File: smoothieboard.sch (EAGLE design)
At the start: 235 parts, among them IC1 LPC1769, IC10 LM1117-3.3V, IC11 78L12F, IC2 A4982, IC3 A4982, IC4 MCP44X1, IC5 A4982, IC6 A4982, J10 POWER_JACKSMD, Q1 BSL207SP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

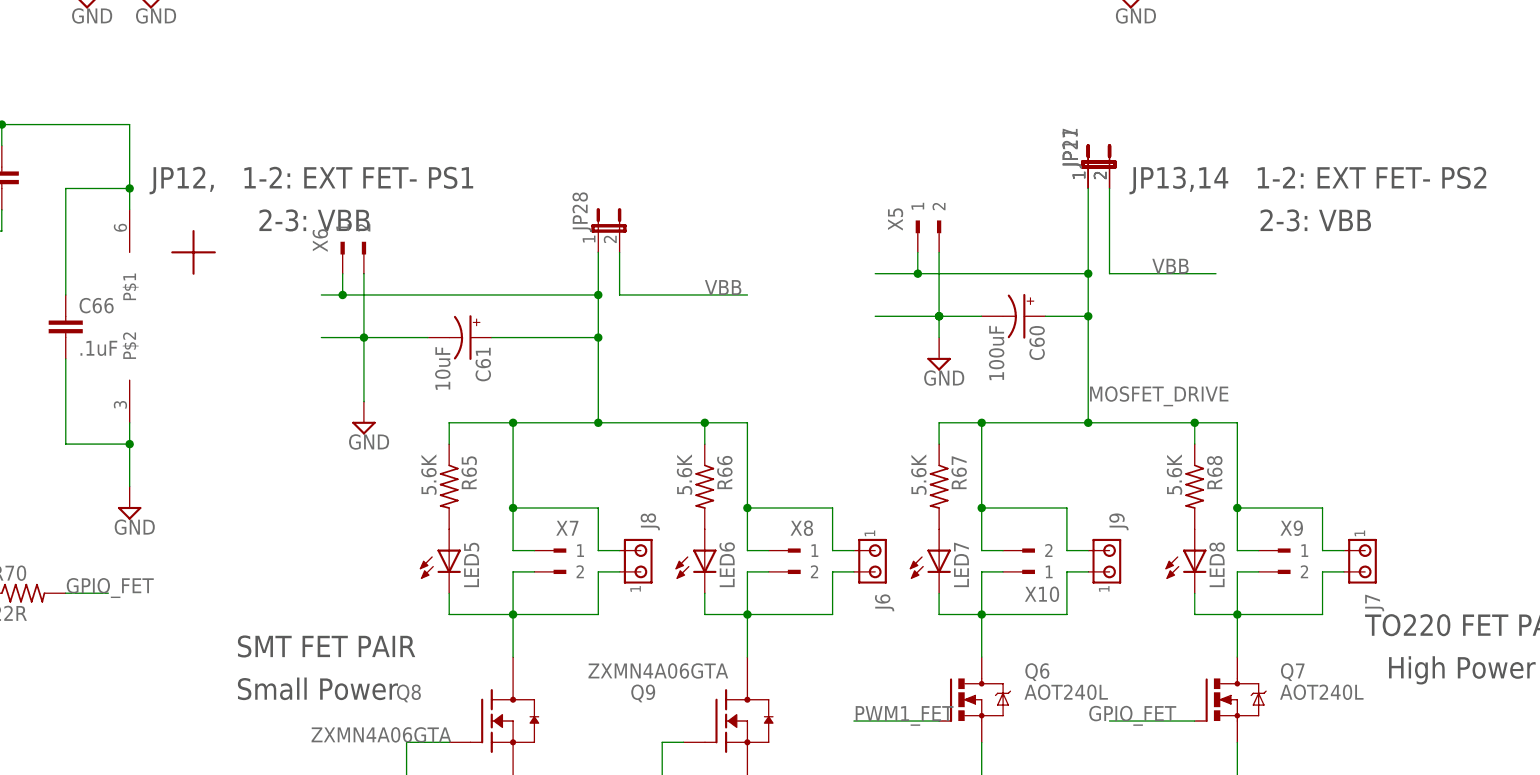
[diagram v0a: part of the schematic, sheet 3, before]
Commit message: Changed Heated Bed connectors
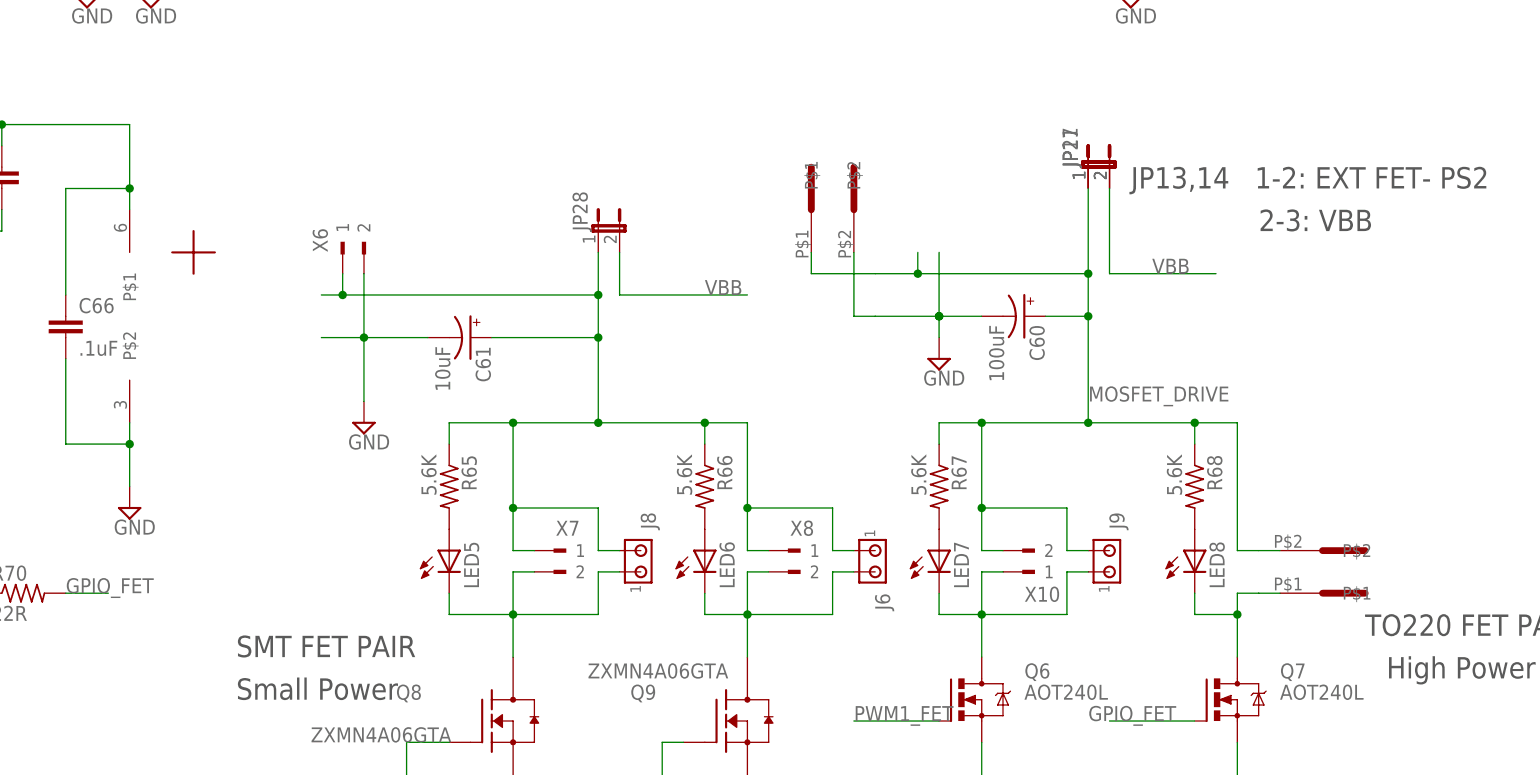
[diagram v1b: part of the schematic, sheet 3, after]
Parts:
- removed J7: (no value), con-amp:MTA02-100
- removed X5, X9: (no value), con-weidmueller-sl35:180G-2
- added U$5, U$6: 5MMCONN, eric_sorensen:5MMCONN
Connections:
- net GND: now also U$5.P$2; no longer X5.2
- net MOSFET_DRIVE: now also U$5.P$1, U$6.P$2; no longer J7.1, X5.1, X9.1
- net N$94: now also U$6.P$1; no longer J7.2, X9.2
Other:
- note removed: "JP12, 1-2: EXT FET- PS1"
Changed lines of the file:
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@@
 <part name="X8" library="con-weidmueller-sl35" deviceset="180G-2" device=""/>
 <part name="X10" library="con-weidmueller-sl35" deviceset="180G-2" device=""/>
-<part name="X9" library="con-weidmueller-sl35" deviceset="180G-2" device=""/>
 <part name="X6" library="con-weidmueller-sl35" deviceset="180G-2" device=""/>
-<part name="X5" library="con-weidmueller-sl35" deviceset="180G-2" device=""/>
 <part name="U$1" library="Geos" deviceset="ETH1506S" device=""/>
 <part name="JP28" library="jumper" deviceset="JP1E" device=""/>
@@
 <part name="J6" library="con-amp" deviceset="MTA02-100" device=""/>
 <part name="J9" library="con-amp" deviceset="MTA02-100" device=""/>
-<part name="J7" library="con-amp" deviceset="MTA02-100" device=""/>
 <part name="JP17" library="SparkFun" deviceset="M03" device="PTH"/>
 <part name="JP18" library="SparkFun" deviceset="M03" device="PTH"/>
@@
 <part name="U$3" library="SparkFun" deviceset="5V" device=""/>
 <part name="U$4" library="SparkFun" deviceset="5V" device=""/>
+<part name="U$5" library="eric_sorensen" deviceset="5MMCONN" device=""/>
+<part name="U$6" library="eric_sorensen" deviceset="5MMCONN" device=""/>
 </parts>
 <sheets>
@@
 <wire x1="342.9" y1="3.81" x2="383.54" y2="3.81" width="0.1524" layer="97"/>
 <wire x1="383.54" y1="3.81" x2="383.54" y2="8.128" width="0.1524" layer="97"/>
-<text x="200.66" y="134.62" size="2.54" layer="97">JP12,   1-2: EXT FET- PS1</text>
 <text x="317.5" y="134.62" size="2.54" layer="97">JP13,14   1-2: EXT FET- PS2</text>
-<text x="213.36" y="129.54" size="2.54" layer="97">2-3: VBB </text>
 <text x="332.74" y="129.54" size="2.54" layer="97">2-3: VBB </text>
 <text x="210.82" y="78.74" size="2.54" layer="97">SMT FET PAIR</text>
@@
 <instance part="X8" gate="G$1" x="276.86" y="91.44"/>
 <instance part="X10" gate="G$1" x="304.8" y="88.9" rot="MR180"/>
-<instance part="X9" gate="G$1" x="335.28" y="91.44"/>
 <instance part="X6" gate="G$1" x="223.52" y="127" rot="R90"/>
-<instance part="X5" gate="G$1" x="292.1" y="129.54" rot="R90"/>
 <instance part="U$1" gate="G$1" x="144.78" y="45.72" rot="R270"/>
 <instance part="JP28" gate="A" x="254" y="129.54"/>
@@
 <instance part="J6" gate="G$1" x="287.02" y="91.44" rot="R270"/>
 <instance part="J9" gate="G$1" x="314.96" y="88.9" rot="MR90"/>
-<instance part="J7" gate="G$1" x="345.44" y="91.44" rot="R270"/>
 <instance part="R65" gate="G$1" x="236.22" y="99.06" rot="R270"/>
 <instance part="LED5" gate="G$1" x="236.22" y="91.44"/>
@@
 <instance part="IC11" gate="G$1" x="170.18" y="142.24"/>
 <instance part="U$3" gate="G$1" x="43.18" y="38.1"/>
+<instance part="U$5" gate="G$1" x="284.48" y="132.08" rot="R90"/>
+<instance part="U$6" gate="G$1" x="340.36" y="91.44" rot="MR180"/>
 </instances>
 <busses>
@@
 <pinref part="SUPPLY24" gate="GND" pin="GND"/>
 <pinref part="C60" gate="G$1" pin="-"/>
-<pinref part="X5" gate="G$1" pin="2"/>
+<pinref part="U$5" gate="G$1" pin="P$2"/>
+<wire x1="284.48" y1="127" x2="284.48" y2="119.38" width="0.1524" layer="91"/>
+<wire x1="284.48" y1="119.38" x2="287.02" y2="119.38" width="0.1524" layer="91"/>
 </segment>
 <segment>
@@
 <net name="N$94" class="0">
 <segment>
-<wire x1="330.2" y1="88.9" x2="332.74" y2="88.9" width="0.4064" layer="91"/>
+<wire x1="330.2" y1="86.36" x2="332.74" y2="86.36" width="0.4064" layer="91"/>
 <wire x1="330.2" y1="78.74" x2="330.2" y2="83.82" width="0.4064" layer="91"/>
-<wire x1="330.2" y1="83.82" x2="330.2" y2="88.9" width="0.4064" layer="91"/>
-<wire x1="342.9" y1="88.9" x2="340.36" y2="88.9" width="0.1524" layer="91"/>
-<wire x1="340.36" y1="88.9" x2="340.36" y2="83.82" width="0.1524" layer="91"/>
-<wire x1="340.36" y1="83.82" x2="330.2" y2="83.82" width="0.1524" layer="91"/>
+<wire x1="330.2" y1="83.82" x2="330.2" y2="86.36" width="0.4064" layer="91"/>
 <junction x="330.2" y="83.82"/>
 <pinref part="Q7" gate="G$1" pin="D"/>
-<pinref part="X9" gate="G$1" pin="2"/>
-<pinref part="J7" gate="G$1" pin="2"/>
 <pinref part="LED8" gate="G$1" pin="C"/>
 <wire x1="325.12" y1="86.36" x2="325.12" y2="83.82" width="0.1524" layer="91"/>
 <wire x1="325.12" y1="83.82" x2="330.2" y2="83.82" width="0.1524" layer="91"/>
+<pinref part="U$6" gate="G$1" pin="P$1"/>
+<wire x1="332.74" y1="86.36" x2="335.28" y2="86.36" width="0.1524" layer="91"/>
 </segment>
 </net>
@@
 <wire x1="307.34" y1="119.38" x2="312.42" y2="119.38" width="0.3048" layer="91"/>
 <wire x1="332.74" y1="91.44" x2="330.2" y2="91.44" width="0.4064" layer="91"/>
-<wire x1="330.2" y1="106.68" x2="330.2" y2="96.52" width="0.4064" layer="91"/>
-<wire x1="330.2" y1="96.52" x2="330.2" y2="91.44" width="0.4064" layer="91"/>
+<wire x1="330.2" y1="106.68" x2="330.2" y2="91.44" width="0.4064" layer="91"/>
 <wire x1="312.42" y1="106.68" x2="325.12" y2="106.68" width="0.4064" layer="91"/>
 <wire x1="325.12" y1="106.68" x2="330.2" y2="106.68" width="0.4064" layer="91"/>
@@
 <wire x1="309.88" y1="91.44" x2="309.88" y2="96.52" width="0.1524" layer="91"/>
 <wire x1="309.88" y1="96.52" x2="299.72" y2="96.52" width="0.1524" layer="91"/>
-<wire x1="342.9" y1="91.44" x2="340.36" y2="91.44" width="0.1524" layer="91"/>
-<wire x1="340.36" y1="91.44" x2="340.36" y2="96.52" width="0.1524" layer="91"/>
-<wire x1="340.36" y1="96.52" x2="330.2" y2="96.52" width="0.1524" layer="91"/>
 <junction x="312.42" y="119.38"/>
 <junction x="312.42" y="106.68"/>
@@
 <junction x="312.42" y="124.46"/>
 <junction x="299.72" y="96.52"/>
-<junction x="330.2" y="96.52"/>
 <pinref part="C60" gate="G$1" pin="+"/>
-<pinref part="X9" gate="G$1" pin="1"/>
-<pinref part="X5" gate="G$1" pin="1"/>
 <pinref part="JP11" gate="A" pin="1"/>
 <pinref part="JP27" gate="A" pin="1"/>
-<pinref part="J7" gate="G$1" pin="1"/>
 <pinref part="X10" gate="G$1" pin="2"/>
 <wire x1="302.26" y1="91.44" x2="299.72" y2="91.44" width="0.4064" layer="91"/>
@@
 <junction x="299.72" y="106.68"/>
 <label x="312.42" y="109.22" size="1.778" layer="95"/>
+<pinref part="U$5" gate="G$1" pin="P$1"/>
+<wire x1="279.4" y1="127" x2="279.4" y2="124.46" width="0.1524" layer="91"/>
+<wire x1="279.4" y1="124.46" x2="287.02" y2="124.46" width="0.1524" layer="91"/>
+<pinref part="U$6" gate="G$1" pin="P$2"/>
+<wire x1="332.74" y1="91.44" x2="335.28" y2="91.44" width="0.1524" layer="91"/>
 </segment>
 <segment>
